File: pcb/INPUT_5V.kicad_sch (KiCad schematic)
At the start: 5 parts

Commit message: updated ethernet
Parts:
- removed D5: BZV55C3V6, Diode_SMD:D_MiniMELF, symbol Diode:BZV55C3V6
- added D12: BAT54S, Package_TO_SOT_SMD:SOT-23, symbol Diode:BAT54S
- renumbered R13 to R35
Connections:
- net RAW is gone; now on an unnamed net: R35.1
- net AGND: now also D12.1 (A)
- net INPUT: now reaches R14.1
- net INPUT: no longer R35.2
- net IO: no longer names the net of R14.2, R15.1
- net IO: no longer C7.1
- new net 3V3: D12.2 (K)
- new net OUTPUT: C7.1, D12.3, R35.2
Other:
- moved on the sheet: C7, R35

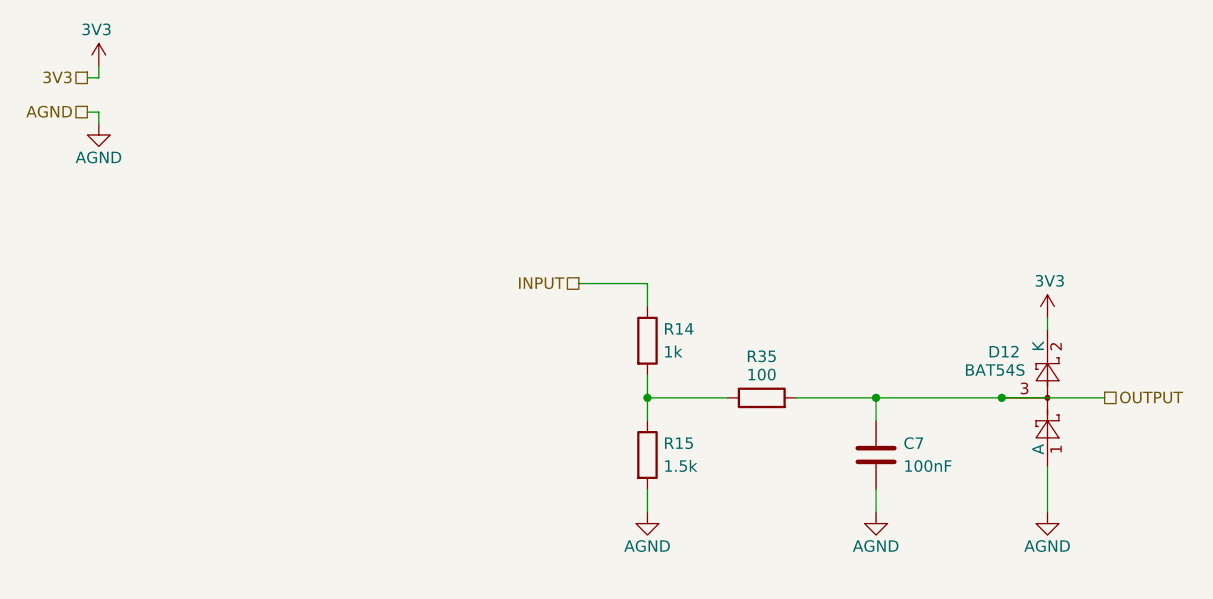
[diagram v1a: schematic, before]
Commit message: reannotated, updated some symbols
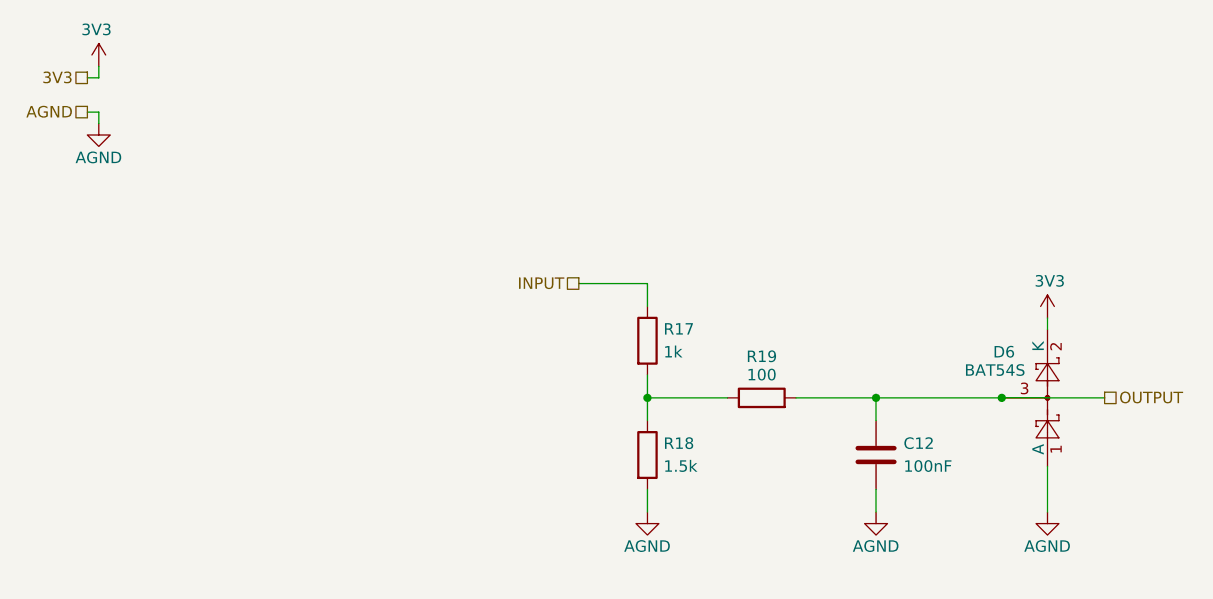
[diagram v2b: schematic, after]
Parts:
- renumbered C7 to C12, D12 to D6, R14 to R17, R15 to R18, R35 to R19

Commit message: removed AGND and added ground garden
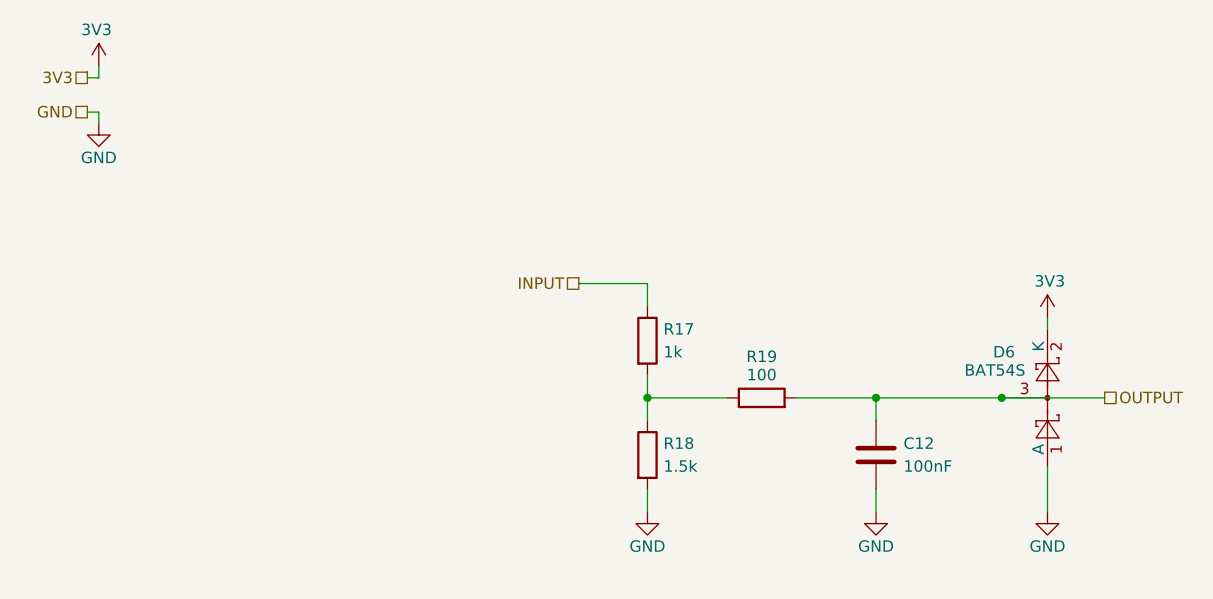
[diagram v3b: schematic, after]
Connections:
- net AGND renamed GND
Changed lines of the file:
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@@
 		)
 	)
-	(hierarchical_label "AGND"
+	(hierarchical_label "GND"
 		(shape passive)
 		(at 26.67 25.4 180)
@@
 			)
 		)
-		(property "Value" "AGND"
+		(property "Value" "GND"
 			(at 114.3 73.66 0)
 			(effects
@@
 			)
 		)
-		(property "Value" "AGND"
+		(property "Value" "GND"
 			(at 88.9 73.66 0)
 			(effects
@@
 			)
 		)
-		(property "Value" "AGND"
+		(property "Value" "GND"
 			(at 133.35 73.66 0)
 			(effects
@@
 			)
 		)
-		(property "Value" "AGND"
+		(property "Value" "GND"
 			(at 27.94 30.48 0)
 			(effects

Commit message: updates from bom release
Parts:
- C12: value 100nF -> 100n
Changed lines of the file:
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@@
 			)
 		)
-		(property "Value" "100nF"
+		(property "Value" "100n"
 			(at 117.348 64.77 0)
 			(effects
